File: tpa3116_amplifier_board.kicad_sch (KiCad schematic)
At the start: 58 parts, among them IC1 TPA3116D2QDADRQ1, J1 control, J2 control, J3 output_right, J4 output_left, J5 power_supply, J6 power_supply

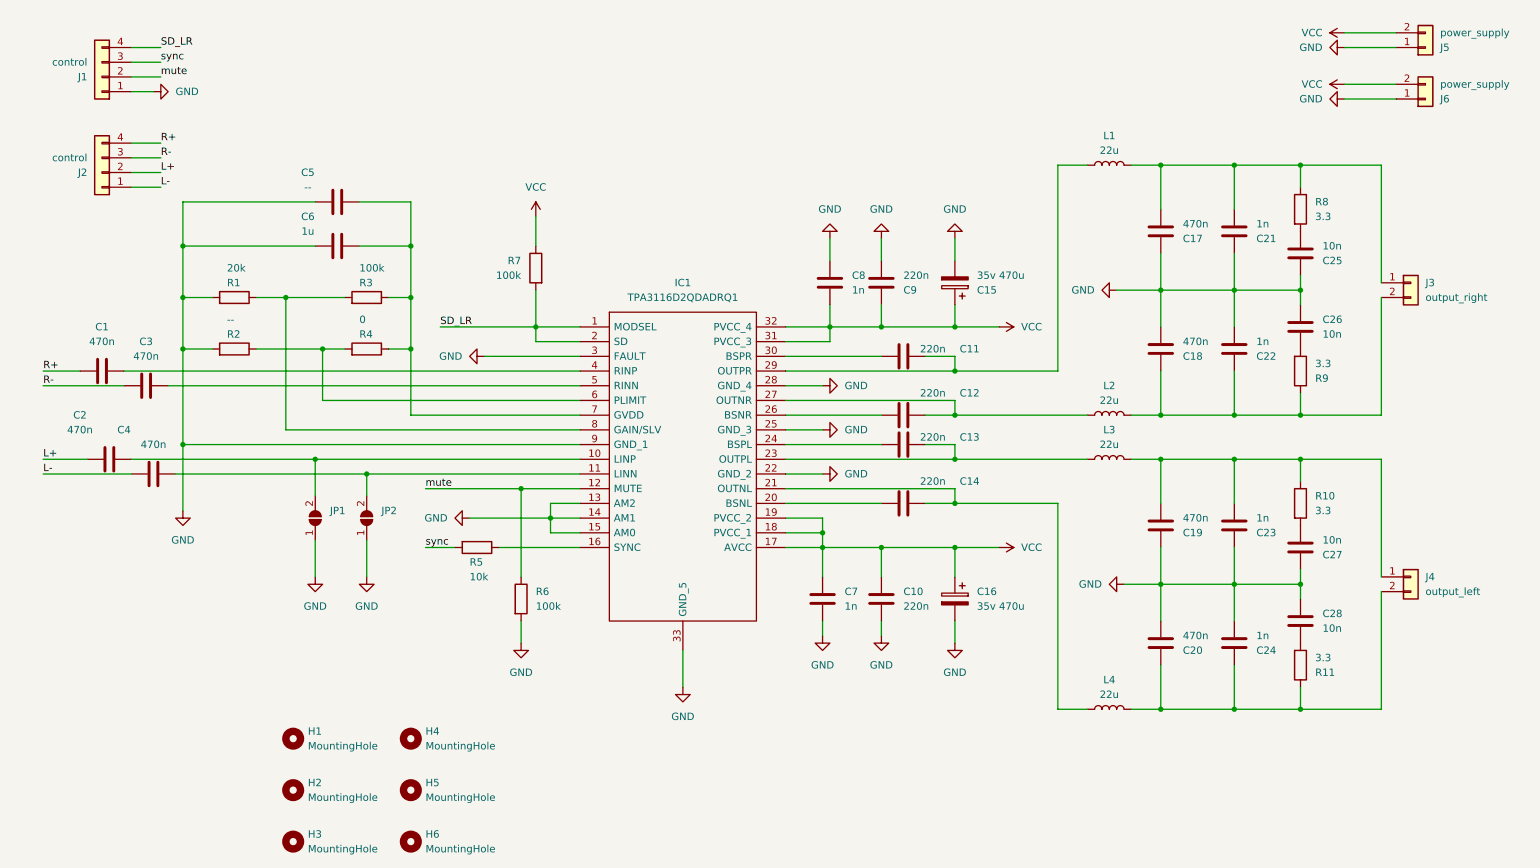
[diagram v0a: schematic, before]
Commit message: Переделал в pbtl версию
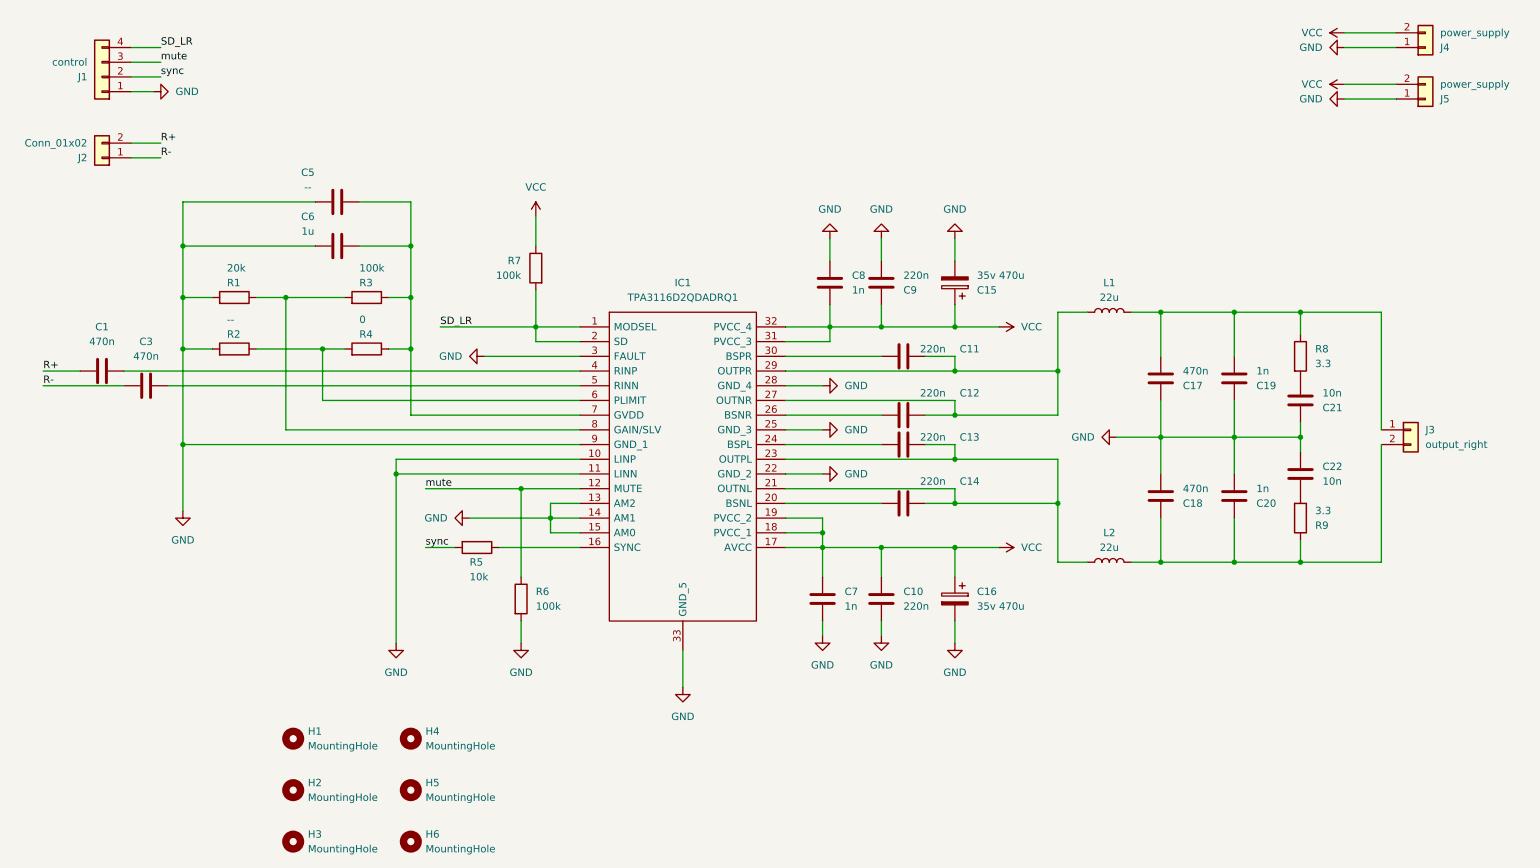
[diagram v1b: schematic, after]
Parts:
- removed C18, C19, C2, C4: 470n, Capacitor_THT:C_Rect_L7.0mm_W4.5mm_P5.00mm, symbol Device:C
- removed C22, C23: 1n, Capacitor_SMD:C_0603_1608Metric, symbol Device:C
- removed C26, C27: 10n, Capacitor_SMD:C_0603_1608Metric, symbol Device:C
- removed J2: control, Connector_Wire:SolderWire-0.25sqmm_1x04_P4.2mm_D0.65mm_OD1.7mm, symbol Connector_Generic:Conn_01x04
- removed J4: output_left, Connector_Wire:SolderWire-1sqmm_1x02_P5.4mm_D1.4mm_OD2.7mm, symbol Connector_Generic:Conn_01x02
- removed JP1, JP2: SolderJumper_2_Open, Jumper:SolderJumper-2_P1.3mm_Open_RoundedPad1.0x1.5mm, symbol Jumper:SolderJumper_2_Open
- removed L2, L3: 22u, Inductor_SMD:L_12x12mm_H8mm, symbol Device:L
- removed R10, R9: 3.3, Resistor_SMD:R_0603_1608Metric, symbol Device:R
- added J2: Conn_01x02, Connector_Wire:SolderWire-0.25sqmm_1x02_P4.2mm_D0.65mm_OD1.7mm, symbol Connector_Generic:Conn_01x02
- renumbered C20 to C18, C21 to C19, C24 to C20, C25 to C21, C28 to C22, J5 to J4, J6 to J5, L4 to L2, R11 to R9
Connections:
- net GND: now also IC1.10 (LINP), IC1.11 (LINN)
- net R+: now also J2.2 (Pin_2)
- net R-: now also J2.1 (Pin_1)
- net mute: now also J1.3 (Pin_3); no longer J1.2 (Pin_2)
- net sync: now also J1.2 (Pin_2); no longer J1.3 (Pin_3)
- net at C18.1, C20.1, L2.2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: now also J3.2 (Pin_2)
- net at C13.1, IC1.23 (OUTPL): now also C14.1, IC1.21 (OUTNL), L2.1
- net at C11.1, IC1.29 (OUTPR), L1.1: now also C12.1, IC1.27 (OUTNR)
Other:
- moved on the sheet: C17, C18, C19, C20, C21, C22, J3, L1, L2, R8, R9

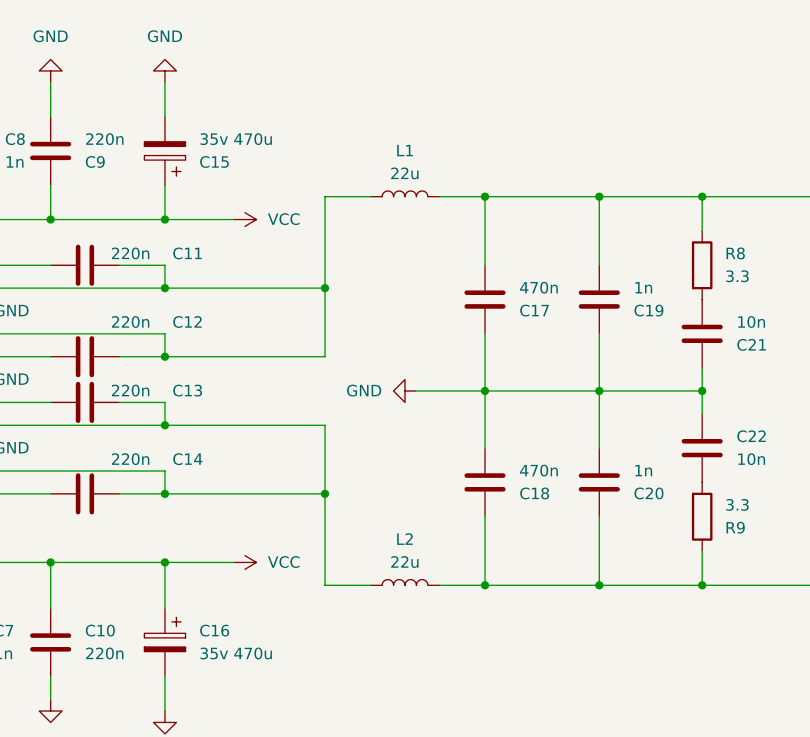
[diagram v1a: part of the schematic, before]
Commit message: Заменил пленочные выводные конденсаторы в фильтре на SMD
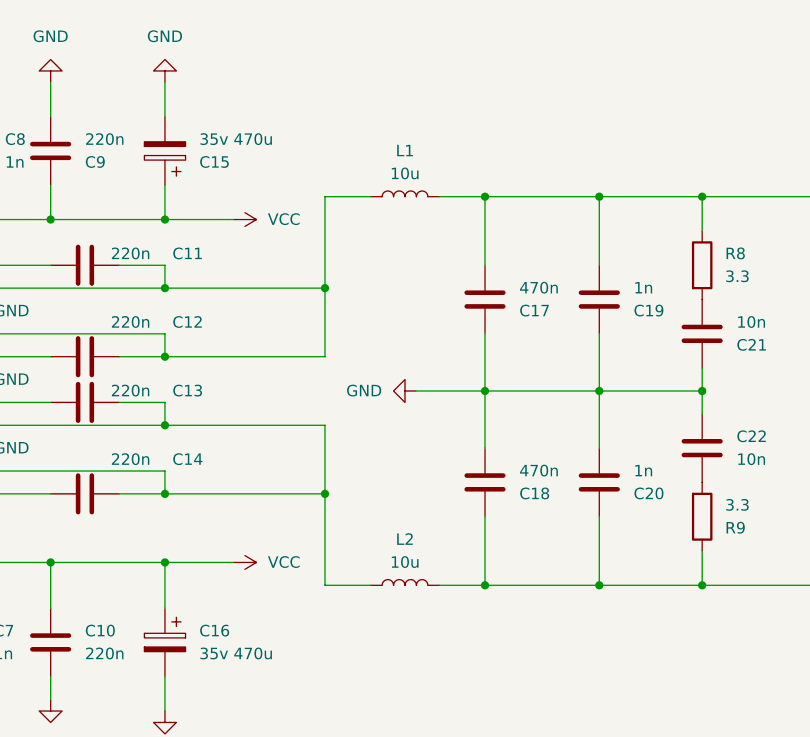
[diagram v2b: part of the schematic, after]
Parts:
- C17, C18: footprint Capacitor_THT:C_Rect_L7.0mm_W4.5mm_P5.00mm -> Capacitor_SMD:C_1812_4532Metric
- L1, L2: value 22u -> 10u
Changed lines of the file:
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@@
       (effects (font (size 1.27 1.27)) (justify left))
     )
-    (property "Footprint" "Capacitor_THT:C_Rect_L7.0mm_W4.5mm_P5.00mm" (at 215.5952 88.9 0)
+    (property "Footprint" "Capacitor_SMD:C_1812_4532Metric" (at 215.5952 88.9 0)
       (effects (font (size 1.27 1.27)) hide)
     )
@@
       (effects (font (size 1.27 1.27)))
     )
-    (property "Value" "22u" (at 205.74 121.92 90)
+    (property "Value" "10u" (at 205.74 121.92 90)
       (effects (font (size 1.27 1.27)))
     )
@@
       (effects (font (size 1.27 1.27)))
     )
-    (property "Value" "22u" (at 205.74 78.74 90)
+    (property "Value" "10u" (at 205.74 78.74 90)
       (effects (font (size 1.27 1.27)))
     )
@@
       (effects (font (size 1.27 1.27)) (justify left))
     )
-    (property "Footprint" "Capacitor_THT:C_Rect_L7.0mm_W4.5mm_P5.00mm" (at 215.5952 109.22 0)
-      (effects (font (size 1.27 1.27)) hide)
-    )
+    (property "Footprint" "Capacitor_SMD:C_1812_4532Metric" (at 215.5952 109.22 0)
+      (effects (font (size 1.27 1.27)) hide)
+    )

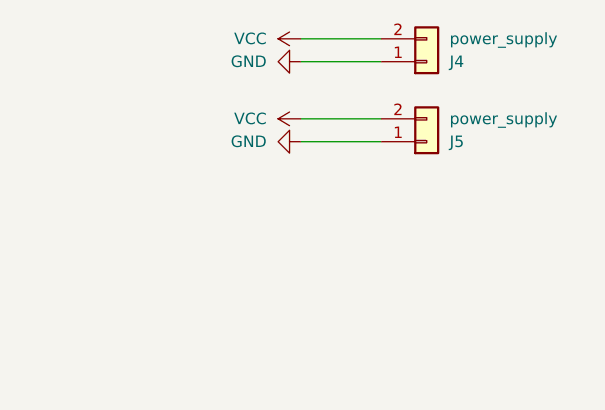
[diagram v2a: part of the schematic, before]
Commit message: Уменьшил размер платы
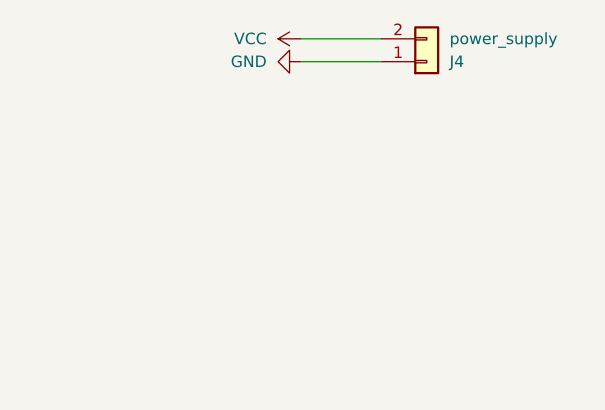
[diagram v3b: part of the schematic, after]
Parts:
- removed J5: power_supply, Connector_Wire:SolderWire-1sqmm_1x02_P5.4mm_D1.4mm_OD2.7mm, symbol Connector_Generic:Conn_01x02
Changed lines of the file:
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@@
-    (stroke (width 0) (type default))
-  )
-  (wire (pts (xy 246.38 41.91) (xy 255.27 41.91))
     (stroke (width 0) (type default))
   )
@@
   )
   (wire (pts (xy 166.37 83.82) (xy 179.07 83.82))
-    (stroke (width 0) (type default))
-  )
-  (wire (pts (xy 246.38 44.45) (xy 255.27 44.45))
     (stroke (width 0) (type default))
   )
@@
     )
   )
-  (symbol (lib_id "Connector_Generic:Conn_01x02") (at 260.35 44.45 0) (mirror x) (unit 1)
-    (in_bom yes) (on_board yes) (dnp no)
-    (property "Reference" "J5" (at 262.89 44.45 0)
-      (effects (font (size 1.27 1.27)) (justify left))
-    )
-    (property "Value" "power_supply" (at 262.89 41.91 0)
-      (effects (font (size 1.27 1.27)) (justify left))
-    )
-    (property "Footprint" "Connector_Wire:SolderWire-1sqmm_1x02_P5.4mm_D1.4mm_OD2.7mm" (at 260.35 44.45 0)
-      (effects (font (size 1.27 1.27)) hide)
-    )
-    (property "Datasheet" "~" (at 260.35 44.45 0)
-      (effects (font (size 1.27 1.27)) hide)
-    )
-    (pin "1")
-    (pin "2")
-    (instances
-      (project "tpa3116_amplifier_board"
-        (path "/d7856d41-bcae-4bc4-ad9f-ba9483713084"
-          (reference "J5") (unit 1)
-        )
-      )
-    )
-  )
   (symbol (lib_id "Device:C") (at 31.75 91.44 90) (unit 1)
     (in_bom yes) (on_board yes) (dnp no) (fields_autoplaced)
@@
         (path "/d7856d41-bcae-4bc4-ad9f-ba9483713084"
           (reference "C5") (unit 1)
-        )
-      )
-    )
-  )
-  (symbol (lib_id "power:GND") (at 246.38 44.45 270) (unit 1)
-    (in_bom yes) (on_board yes) (dnp no) (fields_autoplaced)
-    (property "Reference" "#PWR025" (at 240.03 44.45 0)
-      (effects (font (size 1.27 1.27)) hide)
-    )
-    (property "Value" "GND" (at 242.57 44.45 90)
-      (effects (font (size 1.27 1.27)) (justify right))
-    )
-    (property "Footprint" "" (at 246.38 44.45 0)
-      (effects (font (size 1.27 1.27)) hide)
-    )
-    (property "Datasheet" "" (at 246.38 44.45 0)
-      (effects (font (size 1.27 1.27)) hide)
-    )
-    (pin "1")
-    (instances
-      (project "tpa3116_amplifier_board"
-        (path "/d7856d41-bcae-4bc4-ad9f-ba9483713084"
-          (reference "#PWR025") (unit 1)
         )
       )
@@
         )
       )
-    )
-  )
-  (symbol (lib_id "power:VCC") (at 246.38 41.91 90) (unit 1)
-    (in_bom yes) (on_board yes) (dnp no) (fields_autoplaced)
-    (property "Reference" "#PWR024" (at 250.19 41.91 0)
-      (effects (font (size 1.27 1.27)) hide)
-    )
-    (property "Value" "VCC" (at 242.57 41.91 90)
-      (effects (font (size 1.27 1.27)) (justify left))
-    )
-    (property "Footprint" "" (at 246.38 41.91 0)
-      (effects (font (size 1.27 1.27)) hide)
-    )
-    (property "Datasheet" "" (at 246.38 41.91 0)
-      (effects (font (size 1.27 1.27)) hide)
-    )
-    (pin "1")
-    (instances
-      (project "tpa3116_amplifier_board"
-        (path "/d7856d41-bcae-4bc4-ad9f-ba9483713084"
-          (reference "#PWR024") (unit 1)
-        )
-      )

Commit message: Уменьшил размер коннекторов и подправил переходные отверстия
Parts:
- J3, J4: footprint Connector_Wire:SolderWire-1sqmm_1x02_P5.4mm_D1.4mm_OD2.7mm -> Connector_Wire:SolderWire-0.75sqmm_1x02_P4.8mm_D1.25mm_OD2.3mm
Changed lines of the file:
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@@
       (effects (font (size 1.27 1.27)) (justify left))
     )
-    (property "Footprint" "Connector_Wire:SolderWire-1sqmm_1x02_P5.4mm_D1.4mm_OD2.7mm" (at 260.35 35.56 0)
+    (property "Footprint" "Connector_Wire:SolderWire-0.75sqmm_1x02_P4.8mm_D1.25mm_OD2.3mm" (at 260.35 35.56 0)
       (effects (font (size 1.27 1.27)) hide)
     )
@@
       (effects (font (size 1.27 1.27)) (justify left))
     )
-    (property "Footprint" "Connector_Wire:SolderWire-1sqmm_1x02_P5.4mm_D1.4mm_OD2.7mm" (at 257.81 101.6 0)
-      (effects (font (size 1.27 1.27)) hide)
-    )
+    (property "Footprint" "Connector_Wire:SolderWire-0.75sqmm_1x02_P4.8mm_D1.25mm_OD2.3mm" (at 257.81 101.6 0)
+      (effects (font (size 1.27 1.27)) hide)
+    )

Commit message: Небольшие правки
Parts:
- C1, C3: footprint Capacitor_THT:C_Rect_L7.0mm_W4.5mm_P5.00mm -> Capacitor_THT:C_Rect_L7.0mm_W6.0mm_P5.00mm
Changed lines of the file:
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@@
       (effects (font (size 1.27 1.27)))
     )
-    (property "Footprint" "Capacitor_THT:C_Rect_L7.0mm_W4.5mm_P5.00mm" (at 35.56 90.4748 0)
+    (property "Footprint" "Capacitor_THT:C_Rect_L7.0mm_W6.0mm_P5.00mm" (at 35.56 90.4748 0)
       (effects (font (size 1.27 1.27)) hide)
     )
@@
       (effects (font (size 1.27 1.27)))
     )
-    (property "Footprint" "Capacitor_THT:C_Rect_L7.0mm_W4.5mm_P5.00mm" (at 43.18 93.0148 0)
-      (effects (font (size 1.27 1.27)) hide)
-    )
+    (property "Footprint" "Capacitor_THT:C_Rect_L7.0mm_W6.0mm_P5.00mm" (at 43.18 93.0148 0)
+      (effects (font (size 1.27 1.27)) hide)
+    )

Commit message: Небольшие правки
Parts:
- removed C5: --, Capacitor_SMD:C_0603_1608Metric, symbol Device:C
- removed J1: control, Connector_Wire:SolderWire-0.25sqmm_1x04_P4.2mm_D0.65mm_OD1.7mm, symbol Connector_Generic:Conn_01x04
- removed J2: Conn_01x02, Connector_Wire:SolderWire-0.25sqmm_1x02_P4.2mm_D0.65mm_OD1.7mm, symbol Connector_Generic:Conn_01x02
- added J1: power_supply, Connector_Wire:SolderWire-0.25sqmm_1x02_P4.2mm_D0.65mm_OD1.7mm, symbol Connector_Generic:Conn_01x02
- added J2: Conn_01x04, Connector_Wire:SolderWire-0.25sqmm_1x04_P4.2mm_D0.65mm_OD1.7mm, symbol Connector_Generic:Conn_01x04
- C1: footprint Capacitor_THT:C_Rect_L7.0mm_W6.0mm_P5.00mm -> Capacitor_THT:C_Rect_L7.0mm_W4.5mm_P5.00mm
- C2: renamed from C3; footprint Capacitor_THT:C_Rect_L7.0mm_W6.0mm_P5.00mm -> Capacitor_THT:C_Rect_L7.0mm_W4.5mm_P5.00mm
- renumbered C13 to C10, C14 to C11, C15 to C12, C16 to C13, C17 to C14, C18 to C15, C19 to C16, C20 to C17, C21 to C18, C22 to C19, C6 to C3, C7 to C4, C8 to C5, C9 to C6, C10 to C7, C11 to C8, C12 to C9, J4 to J3, J3 to J4
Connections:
- net GND: now also R8.1, R9.1, J2.1 (Pin_1); no longer C18.1, C19.1
- net R+: now also J1.2 (Pin_2)
- net R-: now also J1.1 (Pin_1)
- net SD_LR: now also J2.4 (Pin_4)
- net mute: now also J2.3 (Pin_3)
- net sync: now also J2.2 (Pin_2)
- net at C15.1, C17.1, J4.2 (Pin_2)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: now also C19.1; no longer R9.1
- net at C14.2, C16.2, J4.1 (Pin_1)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: now also C18.1; no longer R8.1
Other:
- moved on the sheet: C1, C18, C19, C2, J3, R1, R2, R8, R9

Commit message: переделал на разъемы
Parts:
- J1: footprint Connector_Wire:SolderWire-0.25sqmm_1x02_P4.2mm_D0.65mm_OD1.7mm -> Connector_JST:JST_EH_B2B-EH-A_1x02_P2.50mm_Vertical
- J2: footprint Connector_Wire:SolderWire-0.25sqmm_1x04_P4.2mm_D0.65mm_OD1.7mm -> Connector_JST:JST_EH_B4B-EH-A_1x04_P2.50mm_Vertical
- J3, J4: footprint Connector_Wire:SolderWire-0.75sqmm_1x02_P4.8mm_D1.25mm_OD2.3mm -> Connector_JST:JST_VH_B2P-VH-B_1x02_P3.96mm_Vertical
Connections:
- net at C14.2, C16.2, C18.1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: now also J4.2 (Pin_2); no longer J4.1 (Pin_1)
- net at C15.1, C17.1, C19.1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: now also J4.1 (Pin_1); no longer J4.2 (Pin_2)
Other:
- moved on the sheet: J4
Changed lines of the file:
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@@
     (stroke (width 0) (type default))
   )
-  (wire (pts (xy 252.73 104.14) (xy 252.73 124.46))
+  (wire (pts (xy 252.73 102.87) (xy 252.73 124.46))
     (stroke (width 0) (type default))
   )
@@
     (stroke (width 0) (type default))
   )
-  (wire (pts (xy 252.73 81.28) (xy 252.73 101.6))
+  (wire (pts (xy 252.73 81.28) (xy 252.73 100.33))
     (stroke (width 0) (type default))
   )
@@
       (effects (font (size 1.27 1.27)) (justify left))
     )
-    (property "Footprint" "Connector_Wire:SolderWire-0.25sqmm_1x02_P4.2mm_D0.65mm_OD1.7mm" (at 45.72 34.29 0)
+    (property "Footprint" "Connector_JST:JST_EH_B2B-EH-A_1x02_P2.50mm_Vertical" (at 45.72 34.29 0)
       (effects (font (size 1.27 1.27)) hide)
     )
@@
       (effects (font (size 1.27 1.27)) (justify left))
     )
-    (property "Footprint" "Connector_Wire:SolderWire-0.75sqmm_1x02_P4.8mm_D1.25mm_OD2.3mm" (at 242.57 49.53 0)
+    (property "Footprint" "Connector_JST:JST_VH_B2P-VH-B_1x02_P3.96mm_Vertical" (at 242.57 49.53 0)
       (effects (font (size 1.27 1.27)) hide)
     )
@@
       (effects (font (size 1.27 1.27)) (justify left))
     )
-    (property "Footprint" "Connector_Wire:SolderWire-0.25sqmm_1x04_P4.2mm_D0.65mm_OD1.7mm" (at 45.72 46.99 0)
+    (property "Footprint" "Connector_JST:JST_EH_B4B-EH-A_1x04_P2.50mm_Vertical" (at 45.72 46.99 0)
       (effects (font (size 1.27 1.27)) hide)
     )
@@
     )
   )
-  (symbol (lib_id "Connector_Generic:Conn_01x02") (at 257.81 101.6 0) (unit 1)
-    (in_bom yes) (on_board yes) (dnp no) (fields_autoplaced)
-    (property "Reference" "J4" (at 260.35 101.6 0)
-      (effects (font (size 1.27 1.27)) (justify left))
-    )
-    (property "Value" "output_right" (at 260.35 104.14 0)
-      (effects (font (size 1.27 1.27)) (justify left))
-    )
-    (property "Footprint" "Connector_Wire:SolderWire-0.75sqmm_1x02_P4.8mm_D1.25mm_OD2.3mm" (at 257.81 101.6 0)
-      (effects (font (size 1.27 1.27)) hide)
-    )
-    (property "Datasheet" "~" (at 257.81 101.6 0)
-      (effects (font (size 1.27 1.27)) hide)
-    )
+  (symbol (lib_id "Connector_Generic:Conn_01x02") (at 257.81 102.87 0) (mirror x) (unit 1)
+    (in_bom yes) (on_board yes) (dnp no)
+    (property "Reference" "J4" (at 260.35 102.87 0)
+      (effects (font (size 1.27 1.27)) (justify left))
+    )
+    (property "Value" "output_right" (at 260.35 100.33 0)
+      (effects (font (size 1.27 1.27)) (justify left))
+    )
+    (property "Footprint" "Connector_JST:JST_VH_B2P-VH-B_1x02_P3.96mm_Vertical" (at 257.81 102.87 0)
+      (effects (font (size 1.27 1.27)) hide)
+    )
+    (property "Datasheet" "~" (at 257.81 102.87 0)
+      (effects (font (size 1.27 1.27)) hide)
+    )
